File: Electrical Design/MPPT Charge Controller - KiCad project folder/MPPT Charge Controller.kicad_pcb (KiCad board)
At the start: 4 copper layers, 35.6 x 60 mm, 106 parts, among them Q1 SI7272DP, Q3 2N7002, U2 AP63203WU, U3 ACS712-20A, U4 ACS712-20A, U5 MCP4018

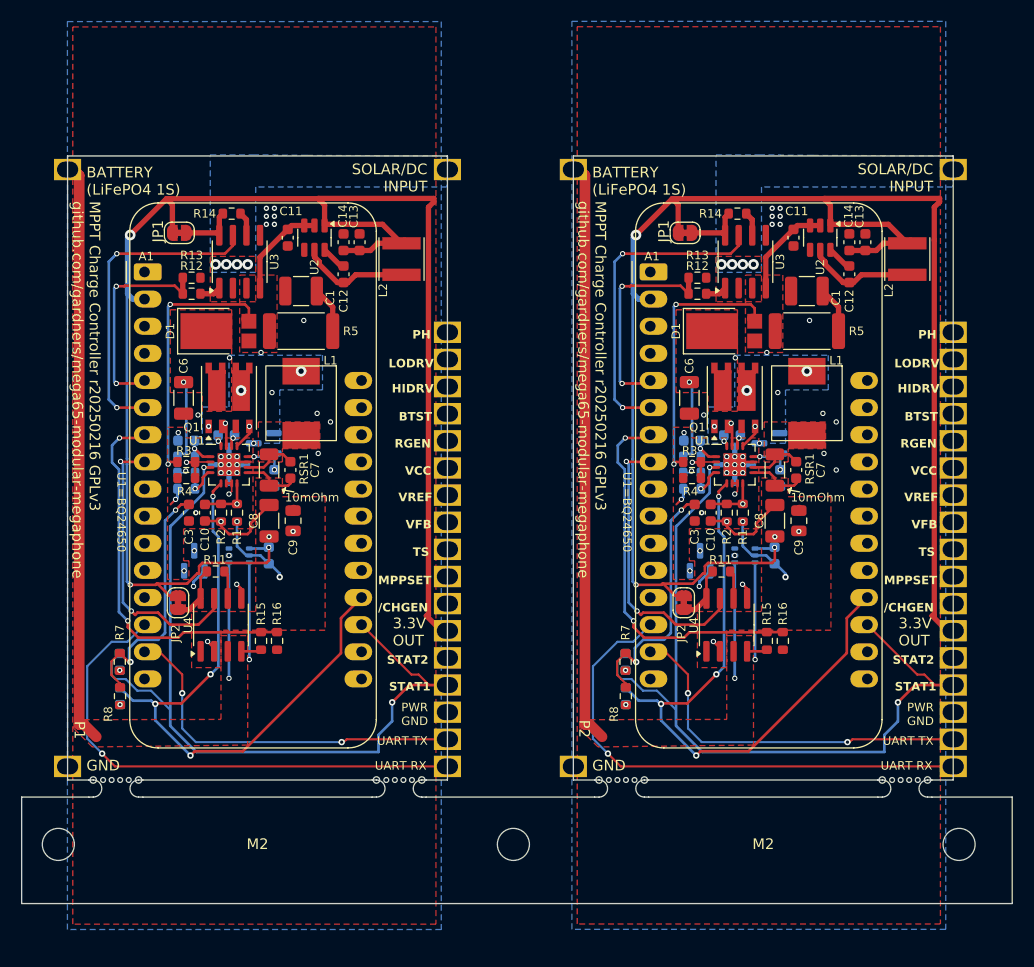
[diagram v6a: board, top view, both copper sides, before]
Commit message: prepare for initial fabrication: No castellation, single instance
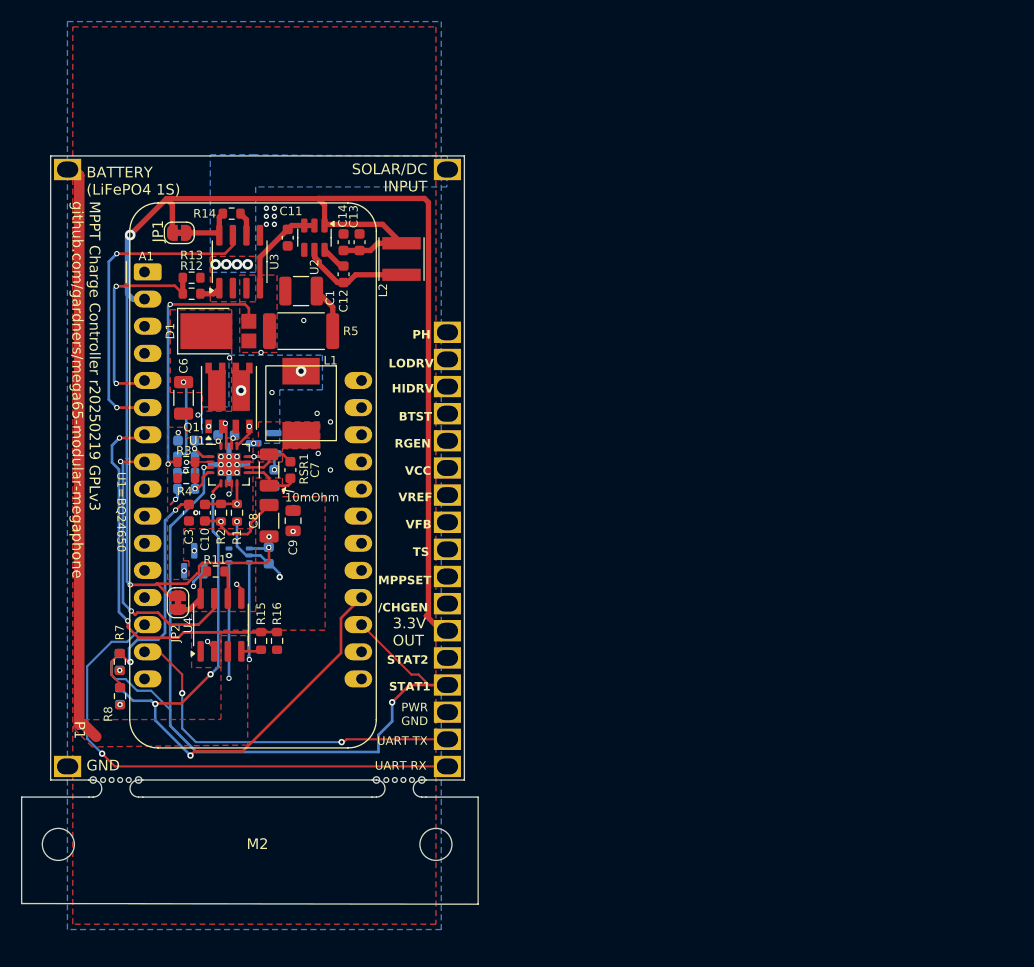
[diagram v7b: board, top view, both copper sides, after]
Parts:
- removed the A1 at (157.2, 98.5)
- removed the C1 at (161.7, 81.2)
- removed the C10 at (152.7, 102.0)
- removed the C11 at (160.5, 76.2)
- removed the C12 at (165.7, 79.6)
- removed the C13 at (167.2, 76.6)
- removed the C14 at (165.7, 76.6)
- removed the C15 at (158.7, 106.0)
- removed the C2 at (151.0, 95.2)
- removed the C3 at (151.2, 102.0)
- removed the C4 at (159.2, 98.7)
- removed the C5 at (154.7, 94.7)
- removed the C6 at (150.7, 91.2)
- removed the C7 at (160.7, 98.0)
- removed the C8 at (158.7, 102.7)
- removed the C9 at (161.0, 102.7)
- removed the D1 at (154.0, 85.0)
- removed the D2 at (158.2, 95.5)
- removed the D3 at (144.8, 115.9)
- removed the D4 at (144.8, 119.1)
- removed the JP1 at (150.3, 75.8)
- removed the JP2 at (150.2, 110.4)
- removed the L1 at (161.7, 91.7)
- removed the L2 at (171.1, 78.2)
- removed the M2 at (157.6, 97.8)
- removed the NT1 at (156.2, 97.5)
- removed the NT2 at (155.0, 96.2)
- removed the NT3 at (153.7, 97.5)
- removed the NT4 at (155.0, 98.7)
- removed the Q1 at (155.0, 91.2)
- removed the Q3 at (151.7, 106.5)
- removed the R1 at (155.7, 102.0)
- removed the R10 at (151.0, 99.7)
- removed the R11 at (153.7, 107.5)
- removed the R12 at (151.5, 81.5)
- removed the R13 at (151.5, 80.0)
- removed the R14 at (155.2, 74.0)
- removed the R15 at (158.0, 114.0)
- removed the R16 at (159.5, 114.0)
- removed the R2 at (154.2, 102.0)
- removed the R3 at (151.0, 97.2)
- removed the R4 at (151.0, 98.7)
- removed the R5 at (161.7, 85.0)
- removed the R6 at (151.0, 96.7)
- removed the R7 at (144.8, 115.9)
- removed the R8 at (144.8, 119.1)
- removed the R9 at (151.0, 98.2)
- removed the RSR1 at (158.7, 98.0)
- removed the U1 at (155.0, 97.5)
- removed the U2 at (163.0, 76.2)
- removed the U3 at (156.0, 78.5)
- removed the U4 at (154.2, 112.5)
- removed the U5 at (155.9, 106.0)
- M2: footprint MegaCastle:MegaCastle2x23-Module-I30.0x53.6-M80000307FFFC-PANEL -> MegaCastle:MegaCastle2x23-Module-I30.0x53.6-M80000307FFFC-PANEL-NIBBLE
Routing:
- net +3.3V: track 294.5 -> 146.3 mm, vias 6 -> 3
- net /STAT1: track 158.2 -> 79.1 mm, vias 4 -> 2
- net /STAT2: track 139.5 -> 69.8 mm, vias 8 -> 4
- net VBAT_OUT: track 113.4 -> 56.7 mm
- net UART_RX: track 97.1 -> 48.6 mm, vias 2 -> 1
- net /VREF: track 97.1 -> 48.5 mm, vias 8 -> 4
- net /MPPSET: track 74.8 -> 37.4 mm, vias 6 -> 3
- net /Battery Voltage: track 71.4 -> 35.7 mm, vias 4 -> 2
- net UART_TX: track 69.9 -> 34.9 mm, vias 4 -> 2
- net /VCC: track 69.5 -> 34.8 mm, vias 8 -> 4
- net /VIN: track 68.5 -> 34.3 mm, vias 4 -> 2
- net PWR_GND: track 65.4 -> 32.7 mm, vias 28 -> 14
- net /TS: track 62.2 -> 31.1 mm, vias 4 -> 2
- net /HIDRV: track 59.9 -> 30.0 mm, vias 4 -> 2
- net /Solar Current: track 59.5 -> 29.8 mm, vias 4 -> 2
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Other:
- board size 35.6 x 60 mm -> 38.7 x 60 mm
- board text added: "${TITLE} r20250219 GPLv3 github.com/gardners/mega65-modular-megaphone"
- board text removed: "${TITLE} r20250216 GPLv3 github.com/gardners/mega65-modular-megaphone"
- board text removed: "P2"
